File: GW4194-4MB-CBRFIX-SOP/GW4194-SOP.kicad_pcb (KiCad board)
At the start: 4 copper layers, 88.9 x 20.3 mm, 20 parts, among them J1 DRAM-SIMM-30, U1 4C4M4, U2 4C4M4, U3 74LVC1G04, U4 74LVC1G74DC, U5 74LVC1G32, U6 XC6206PxxxMR

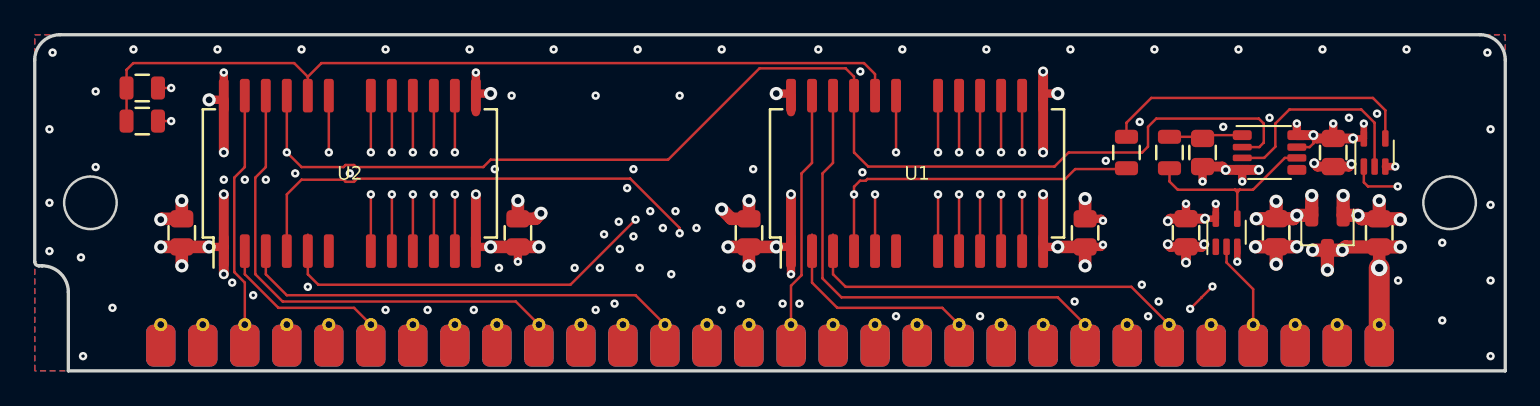
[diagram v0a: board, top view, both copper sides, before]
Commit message: Update to KiCAD 6
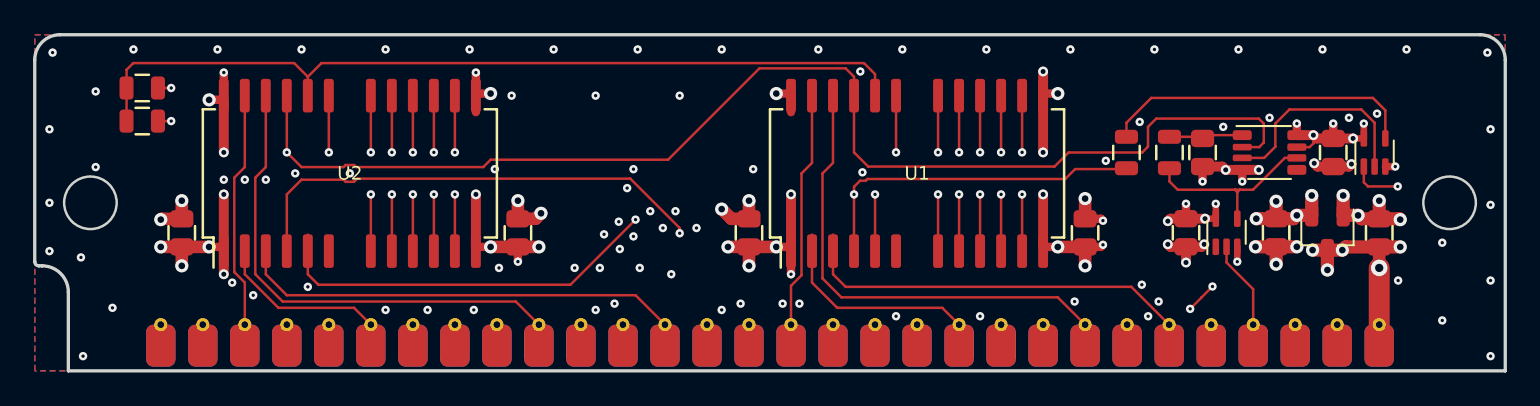
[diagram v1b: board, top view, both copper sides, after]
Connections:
- net /~CASP~ renamed /~{CASP}
- net /~CAS~ renamed /~{CAS}
- net /~OE~ renamed /~{OE}
- net /~RAS~ renamed /~{RAS}
- net /~RWE~ renamed /~{RWE}
- net /~WEE~ renamed /~{WEE}
- net /~WE~ renamed /~{WE}
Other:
- net class Default removed
